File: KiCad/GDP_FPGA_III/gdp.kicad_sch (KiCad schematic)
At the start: 37 parts, among them J1 NKC-Bus, J2 Mini-DIN-6, J3 Mini-DIN-6, J4 AudioJack3, U2 74LVC245, U3 74LVC245, U4 74LVC245

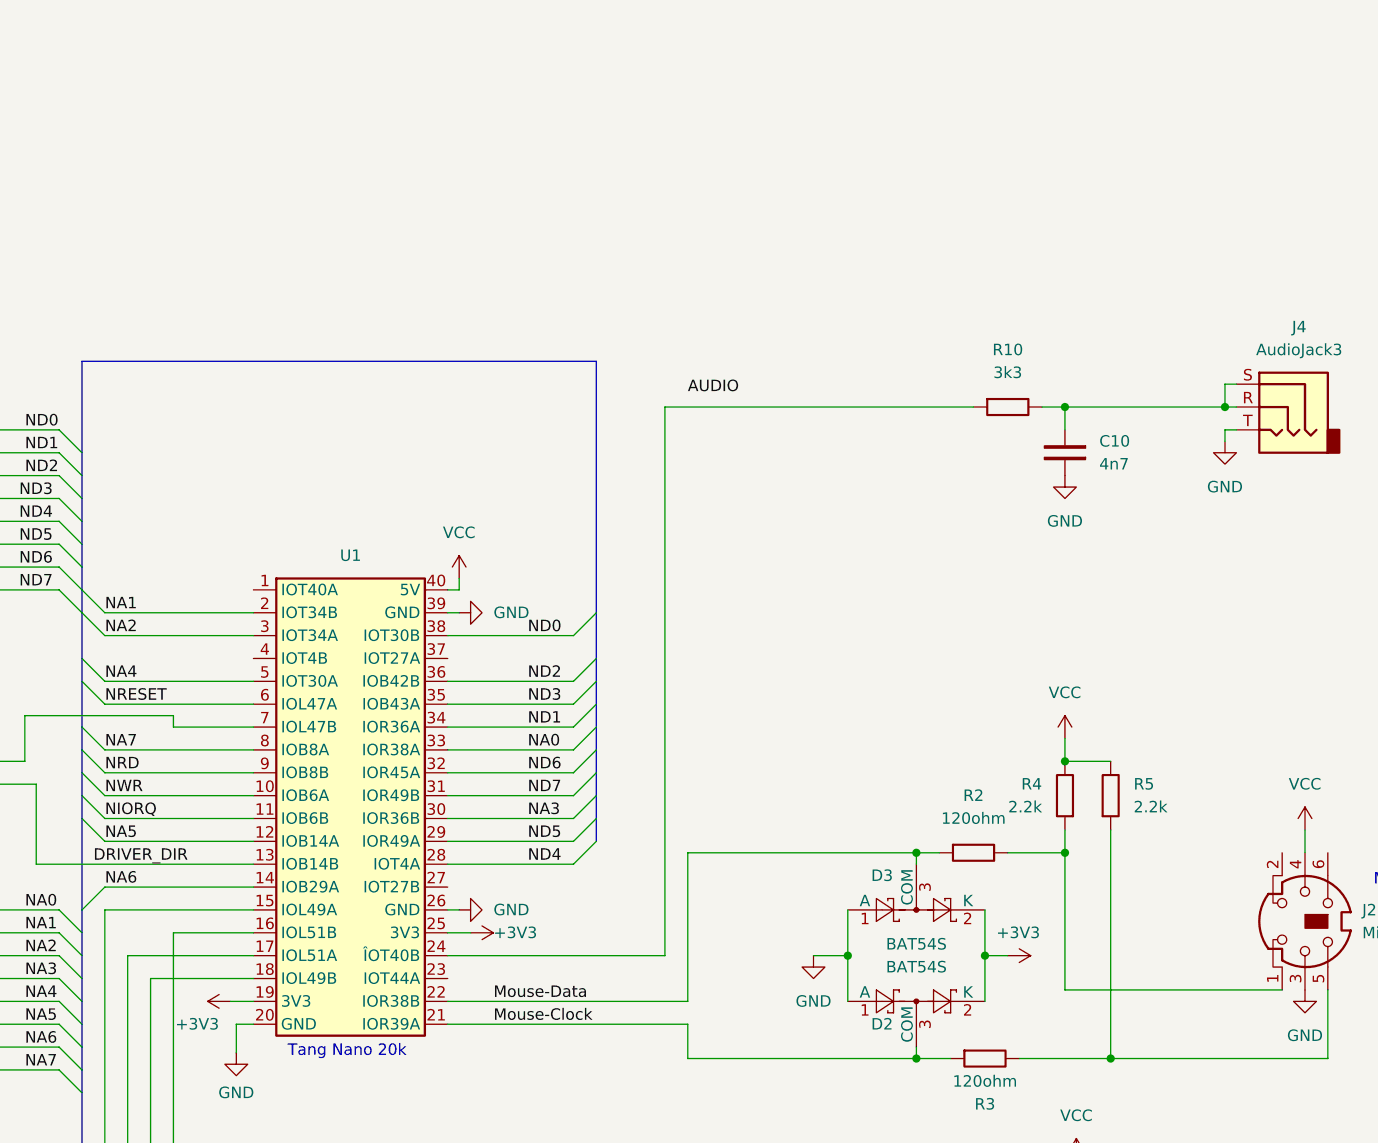
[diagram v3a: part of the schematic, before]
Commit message: New FPGA File with 2nd SD-Card and Patched GP7.10R6 for better compatiblity with SD-Cards
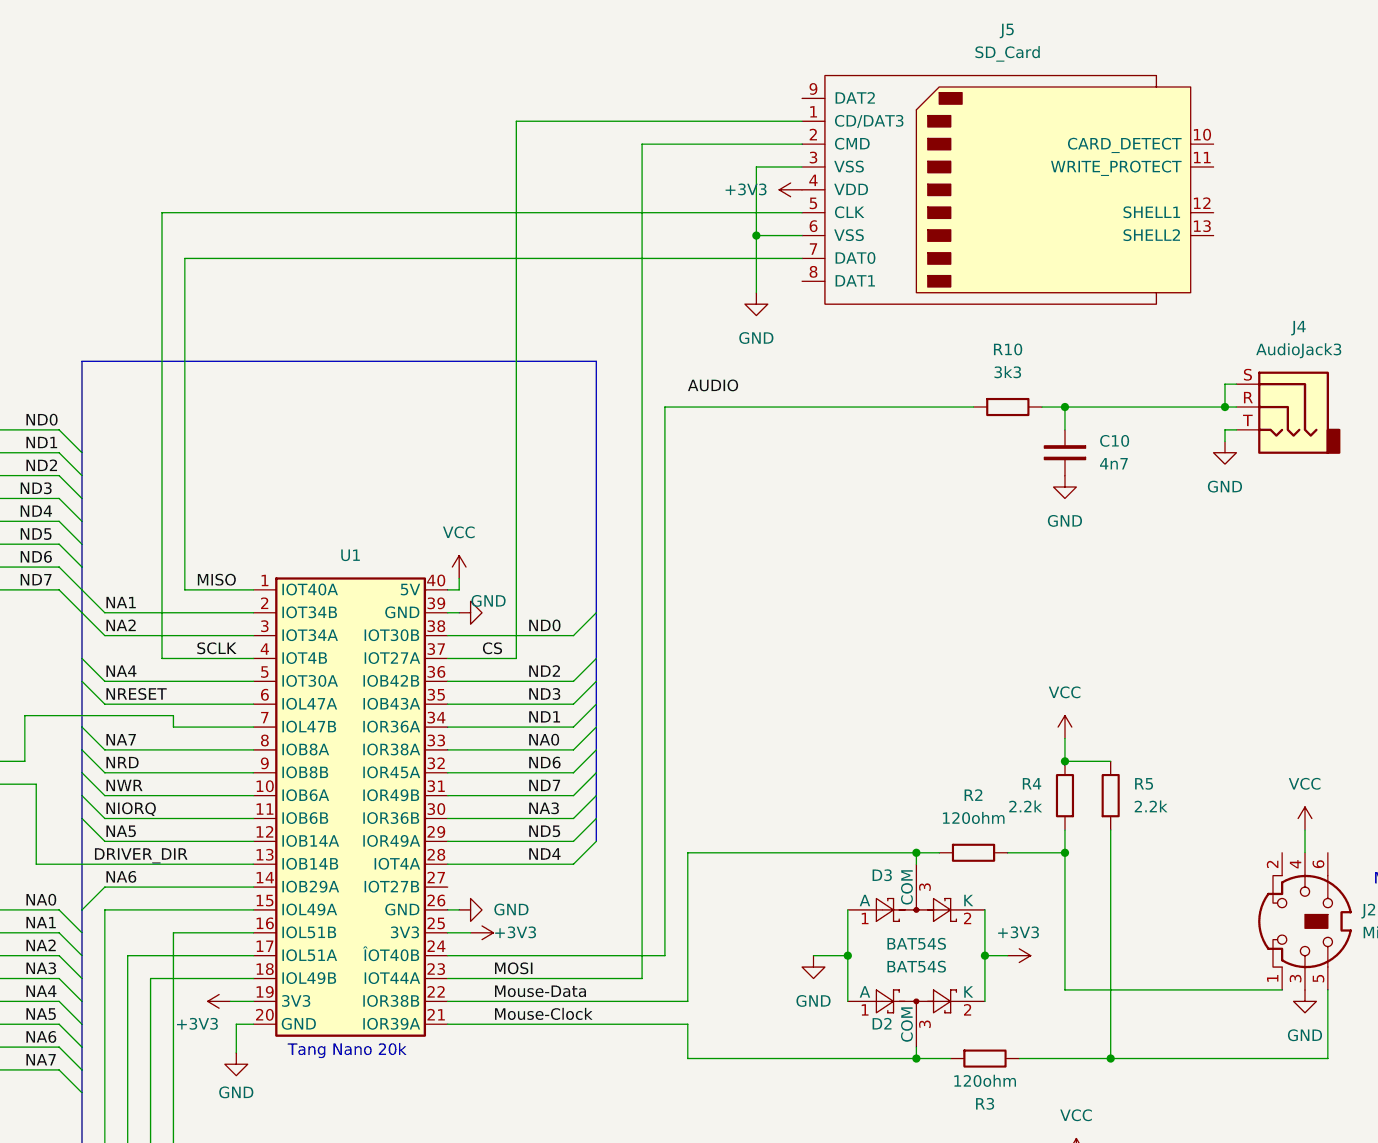
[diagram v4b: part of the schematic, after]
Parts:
- added J5: SD_Card, symbol Connector:SD_Card
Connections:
- net +3V3: now also J5.4 (VDD)
- net GND: now also J5.3 (VSS), J5.6 (VSS)
- net MISO: now reaches U1.1 (IOT40A)
- net MISO: now also J5.7 (DAT0)
- net MOSI: now reaches U1.23 (IOT44A)
- net MOSI: now also J5.2 (CMD)
- net CS: now reaches U1.37 (IOT27A)
- net CS: now also J5.1 (CD/DAT3)
- net SCLK: now reaches U1.4 (IOT4B)
- net SCLK: now also J5.5 (CLK)
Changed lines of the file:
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@@
   (junction (at 331.47 119.38) (diameter 0) (color 0 0 0 0)
+  )
+  (junction (at 321.31 39.37) (diameter 0) (color 0 0 0 0)
   )
   (junction (at 191.77 137.16) (diameter 0) (color 0 0 0 0)
@@
     (stroke (width 0) (type default))
   )
+  (wire (pts (xy 308.61 29.21) (xy 308.61 121.92))
+    (stroke (width 0) (type default))
+  )
   (bus (pts (xy 195.58 76.2) (xy 195.58 111.76))
     (stroke (width 0) (type default))
@@
     (stroke (width 0) (type default))
   )
+  (wire (pts (xy 257.81 41.91) (xy 257.81 78.74))
+    (stroke (width 0) (type default))
+  )
   (bus (pts (xy 93.98 119.38) (xy 93.98 121.92))
     (stroke (width 0) (type default))
@@
     (stroke (width 0) (type default))
   )
+  (wire (pts (xy 321.31 39.37) (xy 326.39 39.37))
+    (stroke (width 0) (type default))
+  )
   (wire (pts (xy 198.12 116.84) (xy 208.28 116.84))
     (stroke (width 0) (type default))
@@
     (stroke (width 0) (type default))
   )
+  (wire (pts (xy 255.27 36.83) (xy 326.39 36.83))
+    (stroke (width 0) (type default))
+  )
   (wire (pts (xy 265.43 119.38) (xy 251.46 119.38))
     (stroke (width 0) (type default))
@@
     (stroke (width 0) (type default))
   )
+  (wire (pts (xy 287.02 86.36) (xy 294.64 86.36))
+    (stroke (width 0) (type default))
+  )
   (bus (pts (xy 93.98 134.62) (xy 93.98 137.16))
     (stroke (width 0) (type default))
@@
     (stroke (width 0) (type default))
   )
+  (wire (pts (xy 265.43 86.36) (xy 255.27 86.36))
+    (stroke (width 0) (type default))
+  )
   (wire (pts (xy 287.02 124.46) (xy 313.69 124.46))
     (stroke (width 0) (type default))
@@
     (stroke (width 0) (type default))
   )
+  (wire (pts (xy 326.39 31.75) (xy 321.31 31.75))
+    (stroke (width 0) (type default))
+  )
   (wire (pts (xy 254 154.94) (xy 254 121.92))
     (stroke (width 0) (type default))
@@
     (stroke (width 0) (type default))
   )
+  (wire (pts (xy 287.02 121.92) (xy 308.61 121.92))
+    (stroke (width 0) (type default))
+  )
+  (wire (pts (xy 308.61 29.21) (xy 326.39 29.21))
+    (stroke (width 0) (type default))
+  )
   (wire (pts (xy 356.87 142.24) (xy 356.87 144.78))
     (stroke (width 0) (type default))
@@
     (stroke (width 0) (type default))
   )
+  (wire (pts (xy 257.81 78.74) (xy 265.43 78.74))
+    (stroke (width 0) (type default))
+  )
   (wire (pts (xy 203.2 83.82) (xy 207.01 83.82))
     (stroke (width 0) (type default))
@@
     (stroke (width 0) (type default))
   )
+  (wire (pts (xy 255.27 86.36) (xy 255.27 36.83))
+    (stroke (width 0) (type default))
+  )
   (bus (pts (xy 246.38 170.18) (xy 246.38 172.72))
     (stroke (width 0) (type default))
   )
+  (wire (pts (xy 321.31 39.37) (xy 321.31 45.72))
+    (stroke (width 0) (type default))
+  )
   (wire (pts (xy 384.81 123.19) (xy 384.81 130.81))
     (stroke (width 0) (type default))
   )
+  (wire (pts (xy 294.64 86.36) (xy 294.64 26.67))
+    (stroke (width 0) (type default))
+  )
   (wire (pts (xy 118.11 214.63) (xy 110.49 214.63))
     (stroke (width 0) (type default))
@@
     (stroke (width 0) (type default))
   )
+  (wire (pts (xy 321.31 31.75) (xy 321.31 39.37))
+    (stroke (width 0) (type default))
+  )
   (wire (pts (xy 347.98 166.37) (xy 347.98 171.45))
     (stroke (width 0) (type default))
@@
     (stroke (width 0) (type default))
   )
+  (wire (pts (xy 326.39 41.91) (xy 257.81 41.91))
+    (stroke (width 0) (type default))
+  )
   (bus (pts (xy 93.98 116.84) (xy 93.98 119.38))
     (stroke (width 0) (type default))
@@
     (stroke (width 0) (type default))
   )
+  (wire (pts (xy 294.64 26.67) (xy 326.39 26.67))
+    (stroke (width 0) (type default))
+  )
   (wire (pts (xy 233.68 124.46) (xy 243.84 124.46))
     (stroke (width 0) (type default))
@@
     (effects (font (size 1.27 1.27)) (justify left bottom))
   )
+  (label "SCLK" (at 259.08 86.36 0) (fields_autoplaced)
+    (effects (font (size 1.27 1.27)) (justify left bottom))
+  )
   (label "{slash}INT" (at 97.79 177.8 0) (fields_autoplaced)
     (effects (font (size 1.27 1.27)) (justify left bottom))
@@
     (effects (font (size 1.27 1.27)) (justify left bottom))
   )
+  (label "MOSI" (at 292.1 121.92 0) (fields_autoplaced)
+    (effects (font (size 1.27 1.27)) (justify left bottom))
+  )
   (label "NA0" (at 295.91 96.52 0) (fields_autoplaced)
     (effects (font (size 1.27 1.27)) (justify left bottom))
@@
     (effects (font (size 1.27 1.27)) (justify left bottom))
   )
+  (label "MISO" (at 259.08 78.74 0) (fields_autoplaced)
+    (effects (font (size 1.27 1.27)) (justify left bottom))
+  )
   (label "D0" (at 189.23 60.96 0) (fields_autoplaced)
     (effects (font (size 1.27 1.27)) (justify left bottom))
@@
   )
   (label "{slash}RESET" (at 96.52 167.64 0) (fields_autoplaced)
+    (effects (font (size 1.27 1.27)) (justify left bottom))
+  )
+  (label "CS" (at 290.83 86.36 0) (fields_autoplaced)
     (effects (font (size 1.27 1.27)) (justify left bottom))
   )
@@
     )
   )
+  (symbol (lib_id "Connector:SD_Card") (at 349.25 34.29 0) (unit 1)
+    (in_bom yes) (on_board yes) (dnp no) (fields_autoplaced)
+    (property "Reference" "J5" (at 349.25 16.51 0)
+      (effects (font (size 1.27 1.27)))
+    )
+    (property "Value" "SD_Card" (at 349.25 19.05 0)
+      (effects (font (size 1.27 1.27)))
+    )
+    (property "Footprint" "" (at 349.25 34.29 0)
+      (effects (font (size 1.27 1.27)) hide)
+    )
+    (property "Datasheet" "http://portal.fciconnect.com/Comergent//fci/drawing/10067847.pdf" (at 349.25 34.29 0)
+      (effects (font (size 1.27 1.27)) hide)
+    )
+    (pin "10")
+    (pin "3")
+    (pin "9")
+    (pin "5")
+    (pin "11")
+    (pin "6")
+    (pin "12")
+    (pin "1")
+    (pin "13")
+    (pin "7")
+    (pin "4")
+    (pin "2")
+    (pin "8")
+    (instances
+      (project "gdp"
+        (path "/7836164f-f628-443b-9592-71227b3bf791"
+          (reference "J5") (unit 1)
+        )
+      )
+    )
+  )
   (symbol (lib_id "PCM_SL_Resistors:2.2k") (at 360.68 101.6 90) (unit 1)
     (in_bom yes) (on_board yes) (dnp no) (fields_autoplaced)
@@
   )
   (symbol (lib_id "power:GND") (at 288.29 81.28 90) (unit 1)
-    (in_bom yes) (on_board yes) (dnp no) (fields_autoplaced)
+    (in_bom yes) (on_board yes) (dnp no)
     (property "Reference" "#PWR08" (at 294.64 81.28 0)
       (effects (font (size 1.27 1.27)) hide)
     )
-    (property "Value" "GND" (at 292.1 81.28 90)
+    (property "Value" "GND" (at 289.56 80.01 90)
       (effects (font (size 1.27 1.27)) (justify right))
     )
@@
         (path "/7836164f-f628-443b-9592-71227b3bf791"
           (reference "#PWR08") (unit 1)
+        )
+      )
+    )
+  )
+  (symbol (lib_id "power:GND") (at 321.31 45.72 0) (unit 1)
+    (in_bom yes) (on_board yes) (dnp no) (fields_autoplaced)
+    (property "Reference" "#PWR035" (at 321.31 52.07 0)
+      (effects (font (size 1.27 1.27)) hide)
+    )
+    (property "Value" "GND" (at 321.31 50.8 0)
+      (effects (font (size 1.27 1.27)))
+    )
+    (property "Footprint" "" (at 321.31 45.72 0)
+      (effects (font (size 1.27 1.27)) hide)
+    )
+    (property "Datasheet" "" (at 321.31 45.72 0)
+      (effects (font (size 1.27 1.27)) hide)
+    )
+    (pin "1")
+    (instances
+      (project "gdp"
+        (path "/7836164f-f628-443b-9592-71227b3bf791"
+          (reference "#PWR035") (unit 1)
         )
       )
@@
         )
       )
+    )
+  )
+  (symbol (lib_id "power:+3V3") (at 326.39 34.29 90) (unit 1)
+    (in_bom yes) (on_board yes) (dnp no) (fields_autoplaced)
+    (property "Reference" "#PWR036" (at 330.2 34.29 0)
+      (effects (font (size 1.27 1.27)) hide)
+    )
+    (property "Value" "+3V3" (at 322.58 34.29 90)
+      (effects (font (size 1.27 1.27)) (justify left))
+    )
+    (property "Footprint" "" (at 326.39 34.29 0)
+      (effects (font (size 1.27 1.27)) hide)
+    )
+    (property "Datasheet" "" (at 326.39 34.29 0)
+      (effects (font (size 1.27 1.27)) hide)
+    )
+    (pin "1")
+    (instances
+      (project "gdp"
+        (path "/7836164f-f628-443b-9592-71227b3bf791"
+          (reference "#PWR036") (unit 1)
+        )
+      )

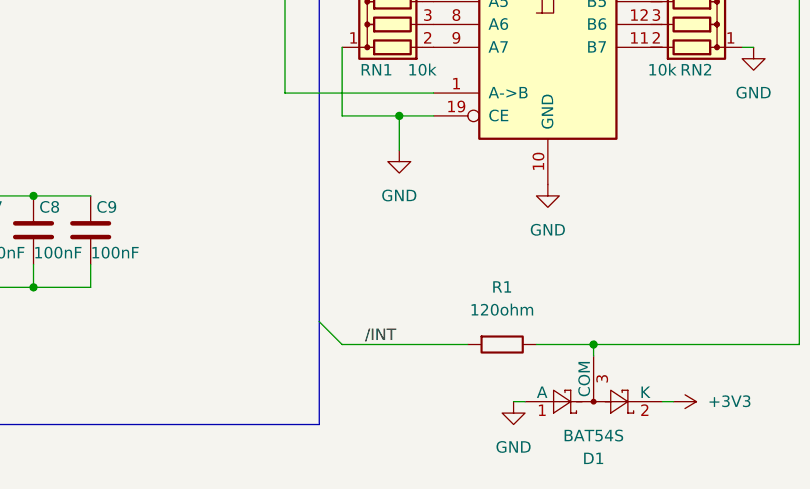
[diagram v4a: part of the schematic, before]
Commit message: update for external Interrupts
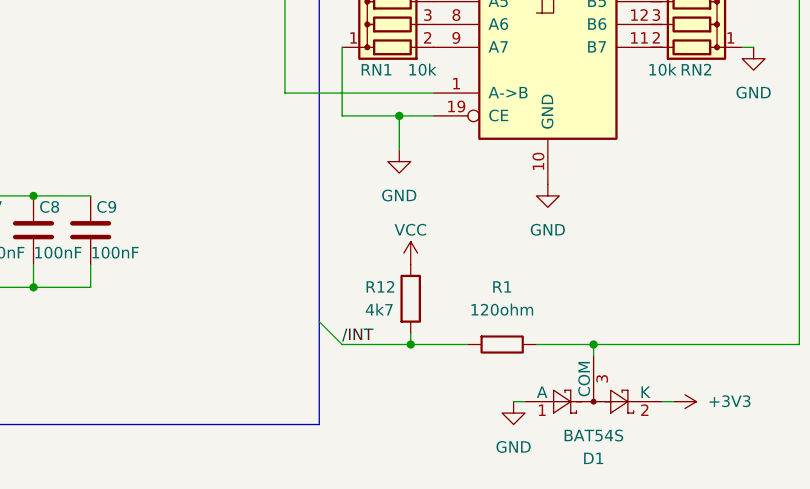
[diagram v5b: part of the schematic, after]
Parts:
- added R12: 4k7, symbol Device:R
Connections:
- net VCC: now also R12.1
- net /INT: now also R12.2
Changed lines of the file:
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@@
   (junction (at 360.68 130.81) (diameter 0) (color 0 0 0 0)
   )
+  (junction (at 205.74 220.98) (diameter 0) (color 0 0 0 0)
+  )
   (junction (at 157.48 204.47) (diameter 0) (color 0 0 0 0)
   )
@@
     (stroke (width 0) (type default))
   )
+  (wire (pts (xy 205.74 220.98) (xy 212.09 220.98))
+    (stroke (width 0) (type default))
+  )
   (wire (pts (xy 102.87 165.1) (xy 96.52 165.1))
     (stroke (width 0) (type default))
@@
     (stroke (width 0) (type default))
   )
-  (wire (pts (xy 198.12 220.98) (xy 212.09 220.98))
-    (stroke (width 0) (type default))
-  )
   (bus (pts (xy 195.58 124.46) (xy 195.58 127))
     (stroke (width 0) (type default))
@@
     (stroke (width 0) (type default))
   )
+  (wire (pts (xy 198.12 220.98) (xy 205.74 220.98))
+    (stroke (width 0) (type default))
+  )
+  (wire (pts (xy 205.74 219.71) (xy 205.74 220.98))
+    (stroke (width 0) (type default))
+  )
   (bus (pts (xy 195.58 66.04) (xy 195.58 68.58))
     (stroke (width 0) (type default))
@@
     (effects (font (size 1.27 1.27)) (justify left bottom))
   )
-  (label "{slash}INT" (at 200.66 220.98 0) (fields_autoplaced)
+  (label "{slash}INT" (at 198.12 220.98 0) (fields_autoplaced)
     (effects (font (size 1.27 1.27)) (justify left bottom))
   )
@@
     )
   )
+  (symbol (lib_id "Device:R") (at 205.74 215.9 0) (unit 1)
+    (in_bom yes) (on_board yes) (dnp no)
+    (property "Reference" "R12" (at 200.66 214.63 0)
+      (effects (font (size 1.27 1.27)) (justify left))
+    )
+    (property "Value" "4k7" (at 200.66 217.17 0)
+      (effects (font (size 1.27 1.27)) (justify left))
+    )
+    (property "Footprint" "" (at 203.962 215.9 90)
+      (effects (font (size 1.27 1.27)) hide)
+    )
+    (property "Datasheet" "~" (at 205.74 215.9 0)
+      (effects (font (size 1.27 1.27)) hide)
+    )
+    (pin "1")
+    (pin "2")
+    (instances
+      (project "gdp"
+        (path "/7836164f-f628-443b-9592-71227b3bf791"
+          (reference "R12") (unit 1)
+        )
+      )
+    )
+  )
   (symbol (lib_id "power:+3V3") (at 262.89 124.46 90) (unit 1)
     (in_bom yes) (on_board yes) (dnp no)
@@
         )
       )
+    )
+  )
+  (symbol (lib_id "power:VCC") (at 205.74 212.09 0) (unit 1)
+    (in_bom yes) (on_board yes) (dnp no)
+    (property "Reference" "#PWR037" (at 205.74 215.9 0)
+      (effects (font (size 1.27 1.27)) hide)
+    )
+    (property "Value" "VCC" (at 205.74 208.28 0)
+      (effects (font (size 1.27 1.27)))
+    )
+    (property "Footprint" "" (at 205.74 212.09 0)
+      (effects (font (size 1.27 1.27)) hide)
+    )
+    (property "Datasheet" "" (at 205.74 212.09 0)
+      (effects (font (size 1.27 1.27)) hide)
+    )
+    (pin "1")
+    (instances
+      (project "gdp"
+        (path "/7836164f-f628-443b-9592-71227b3bf791"
+          (reference "#PWR037") (unit 1)
+        )
+      )
